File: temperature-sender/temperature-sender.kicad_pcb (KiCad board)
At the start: 2 copper layers, 50 x 25 mm, 43 parts, among them IC1 ATTINY2313A-S, K1 SERVO, P1 CONN_01X02, P2 CONN_01X02, P3 CONN_01X02, P6 ISP, P7 CONN_01X03, P8 CONN_01X03, SW1 SW_PUSH, SW2 SW_PUSH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

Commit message: Some more changes, slowly getting there
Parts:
- removed P6: ISP, Socket_Strips:Socket_Strip_Straight_2x03
- removed P7, P8: CONN_01X03, kicad-footprints:Pin_Header_Angled_SMD_1x03
- removed TP_PB0, TP_PB4, TP_PD4, TP_PD5, TP_PD6: TEST_POINT, kicad-footprints:TP_1mm
- removed U4: HT7550-1, Housings_SOT-89:SOT89-3_Housing_Handsoldering
- added C10: 0.1uF, Capacitors_SMD:C_0603_HandSoldering, B.Cu at (143.0, 148.5)
- added C8: 10uF, Capacitors_SMD:C_0603_HandSoldering, F.Cu at (139.5, 138.5)
- added C9: 10uF, Capacitors_SMD:C_0603_HandSoldering, F.Cu at (133.7, 144.8)
- added P4: CONN_01X04, kicad-footprints:Pin_Header_Angled_SMD_1x04, F.Cu at (109.3, 141.5)
- added P5: CONN_01X03, kicad-footprints:Pin_Header_Angled_SMD_1x03, F.Cu at (144.4, 134.6)
- added R1: 47k, Resistors_SMD:R_0603_HandSoldering, B.Cu at (136.3, 109.6)
- added R10: 5k, Resistors_SMD:R_0603_HandSoldering, F.Cu at (117.2, 145.5)
- added TP_PB2: TEST_POINT, kicad-footprints:TP_1mm, B.Cu at (123.7, 139.9)
- added TP_PB3: TEST_POINT, kicad-footprints:TP_1mm, B.Cu at (127.5, 144.7)
- added TP_PD1: TEST_POINT, kicad-footprints:TP_1mm, B.Cu at (123.8, 135.4)
- added TP_PD2: TEST_POINT, kicad-footprints:TP_1mm, B.Cu at (122.3, 135.4)
- C1: value 10uF -> 1uF
- C2, C4: value 1uF -> 10uF
- C3: value C -> 0.1uF; moved to B.Cu
- C5, C7: value 0.1uF -> 10uF
- P1: value CONN_01X02 -> ISP; footprint kicad-footprints:Pin_Header_Angled_SMD_1x02 -> Socket_Strips:Socket_Strip_Straight_2x03
- P3: value CONN_01X02 -> CONN_01X03; footprint kicad-footprints:Pin_Header_Angled_SMD_1x02 -> kicad-footprints:Pin_Header_Angled_SMD_1x03; moved to B.Cu
- R3: value 5k -> 240R
- R4: value 47R -> 1k5
- R5, R6: value 47k -> 47R
- R7: value 5k -> 47k; moved to B.Cu
- R9: value 47R -> 5k
- SW1, SW2: footprint Buttons_Switches_SMD:SW_SPST_PTS645 -> kicad-footprints:4x4x1.5mm_Tactile_Push_Button_SMD; moved to B.Cu
- U1: value MCP1700T-3302E/TT -> AMS1117; footprint Housings_SOT-23_SOT-143_TSOT-6:SOT-23_Handsoldering -> kicad-footprints:SOT-223
- U2: value TMP102 -> LM317L; footprint kicad-footprints:SOT563 -> Housings_TO-92:TO-92_Inline_Narrow_Oval
- U3: value 78L09 -> TMP102; footprint Housings_TO-92:TO-92_Inline_Narrow_Oval -> kicad-footprints:SOT563
- moved C5 101.0 mm to (106.3, 105.5), turned to 0 degrees
- moved C7 87.1 mm to (106.2, 103.6)
- moved R8 76.3 mm to (130.1, 146.7), turned to 180 degrees
- moved R4 59.8 mm to (104.9, 114.9)
- moved R5 58.8 mm to (139.1, 134.4), turned to 180 degrees
- moved R9 54.4 mm to (125.7, 148.4), turned to 270 degrees
- moved R7 52.4 mm to (140.9, 152.8)
- moved C3 41.6 mm to (136.1, 113.9)
- moved R3 40.9 mm to (104.9, 113.0), turned to 0 degrees
- moved U2 40.7 mm to (105.2, 110.5), turned to 90 degrees
- moved U3 34.3 mm to (120.7, 148.5)
- moved P2 31.9 mm to (94.7, 110.8)
- moved C6 28.2 mm to (106.2, 101.5), turned to 0 degrees
- moved C1 27.2 mm to (103.3, 104.5)
- moved P1 26.2 mm to (114.6, 139.6), turned to 90 degrees
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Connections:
- C1 pad 1: +5V -> /Vin_rec
- C3 pad 1: /SERVO_PWR -> GND
- C3 pad 2: GND -> /SW
- C4 pad 1: Net-(C4-Pad1) -> /9v
- C5 pad 1: /RESET -> /9v
- C6 pad 1: +9V -> /9v
- C7 pad 1: GND -> /9v
- C7 pad 2: Net-(C7-Pad2) -> GND
- D1 pad 1: Net-(C4-Pad1) -> /Vin_rec
- D1 pad 2: Net-(D1-Pad2) -> /Vin1
- D2 pad 1: Net-(D2-Pad1) -> /Vin_rec
- D2 pad 2: GND -> /Vin2
- D4 pad 1: Net-(D1-Pad2) -> /Vin2
- D5 pad 1: Net-(C4-Pad1) -> /Vin1
- D5 pad 2: Net-(D2-Pad1) -> GND
- IC1 pad 7: Net-(IC1-Pad7) -> /SW
- K1 pad 3: Net-(K1-Pad3) -> /SERVO_SIG
- P1 pad 1: Net-(D2-Pad1) -> /MISO
- P1 pad 2: Net-(D1-Pad2) -> +3V3
- P2 pad 1: /SDA/MOSI -> /Vin2
- P2 pad 2: /SCL -> /Vin1
- P3 pad 2: +3V3 -> /TX
- R3 pad 1: /ALERT -> /Vadj
- R3 pad 2: +3V3 -> /9v
- R4 pad 1: Net-(K1-Pad3) -> GND
- R4 pad 2: /SERVO1 -> /Vadj
- R5 pad 1: +3V3 -> /SERVO_SIG
- R5 pad 2: /RESET -> /SERVO1
- R6 pad 1: +3V3 -> /SERVO_PWR
- R6 pad 2: Net-(C7-Pad2) -> +3V3
- R7 pad 2: /SCL -> /RESET
- R9 pad 1: /SERVO_PWR -> +3V3
- R9 pad 2: +3V3 -> /SCL
- SW1 pad 1: GND -> /SW
- SW1 pad 2: /RESET -> GND
- SW2 pad 1: Net-(C7-Pad2) -> GND
- SW2 pad 2: GND -> /RESET
- TP_PB1 pad 1: Net-(IC1-Pad13) -> Net-(IC1-Pad12)
- TP_PD3 pad 1: Net-(IC1-Pad7) -> Net-(IC1-Pad11)
- TP_XTAL1 pad 1: Net-(IC1-Pad5) -> Net-(IC1-Pad4)
- TP_XTAL2 pad 1: Net-(IC1-Pad4) -> Net-(IC1-Pad5)
- U1 pad 3: +5V -> /9v
- U2 pad 1: /SCL -> /Vadj
- U2 pad 2: GND -> /9v
- U2 pad 3: /ALERT -> /Vin_rec
- U3 pad 1: +9V -> /SCL
- U3 pad 3: Net-(C4-Pad1) -> /ALERT

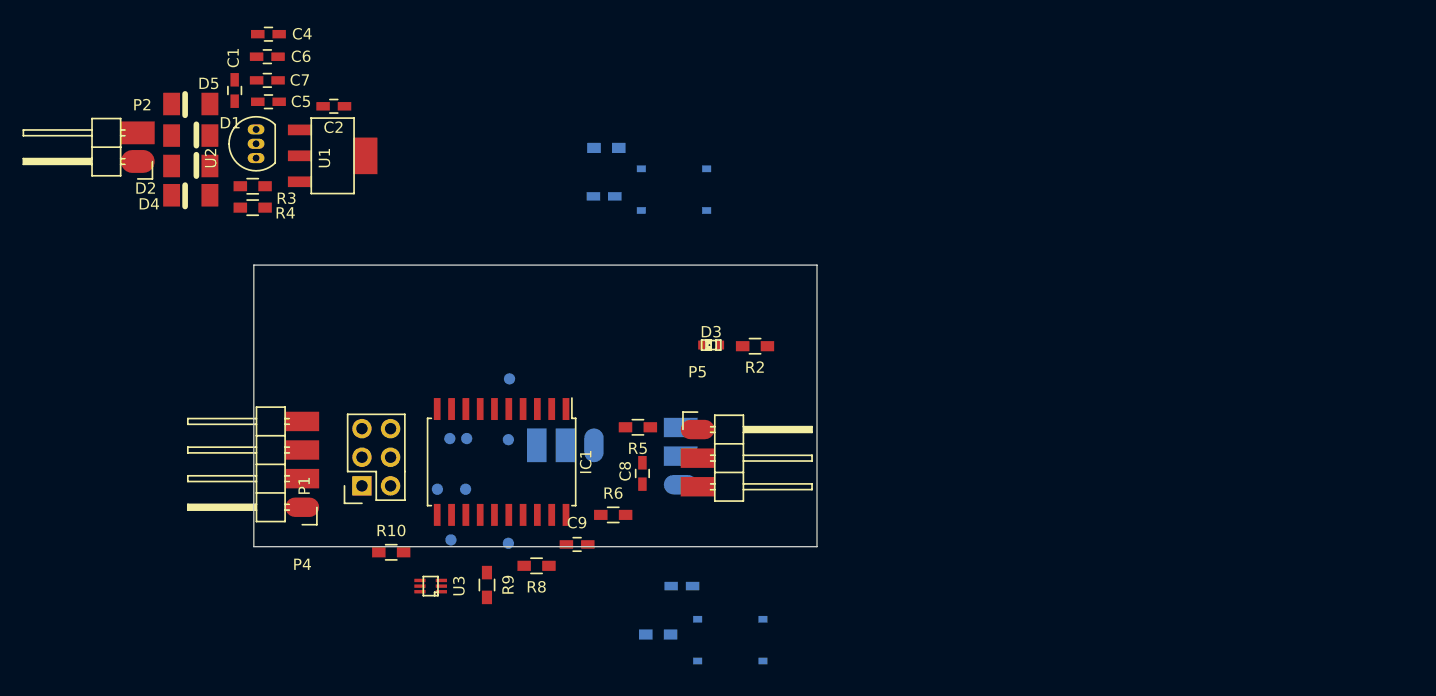
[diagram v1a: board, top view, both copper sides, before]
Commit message: Components placement mostly done
Problem with small temperature footprint. I like to have wider
power traces, but then it can't route this chip. Must figure out how
to solve it in KiCad.
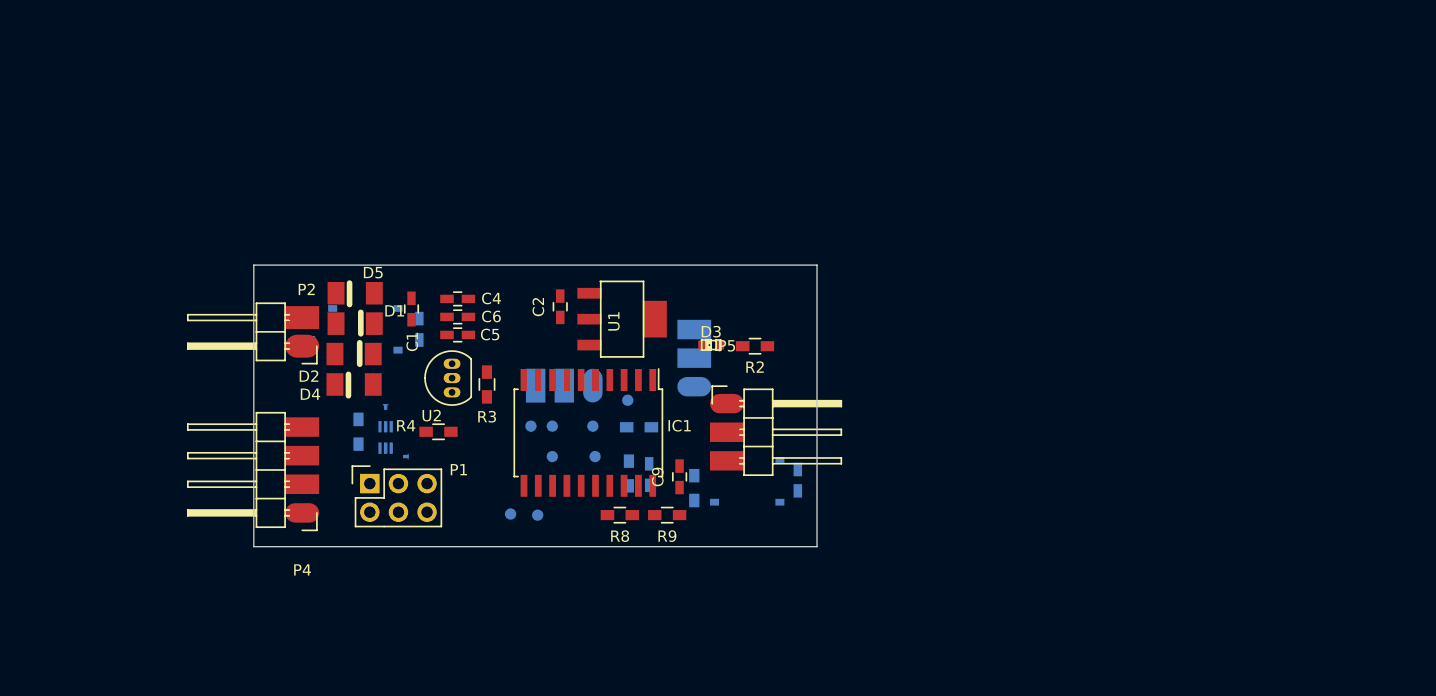
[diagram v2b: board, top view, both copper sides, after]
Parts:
- removed C7: 10uF, Capacitors_SMD:C_0603_HandSoldering
- added P6: 03mmTo05mm, kicad-footprints:03mmTo05mm, B.Cu at (116.7, 132.7)
- added P7: 03mmTo05mm, kicad-footprints:03mmTo05mm, B.Cu at (118.4, 137.0)
- C8, R10, R5, R6, U3: moved to B.Cu
- moved SW2 42.6 mm to (114.9, 125.7)
- moved R7 41.0 mm to (110.0, 125.8), turned to 90 degrees
- moved C10 32.6 mm to (119.7, 125.7), turned to 270 degrees
- moved R1 31.2 mm to (144.1, 139.8), turned to 270 degrees
- moved C3 30.5 mm to (153.3, 139.1), turned to 270 degrees
- moved U1 29.5 mm to (137.7, 124.8)
- moved C4 28.9 mm to (123.1, 123.0)
- moved C6 28.6 mm to (123.1, 124.6)
- moved R3 27.2 mm to (125.7, 130.6), turned to 90 degrees
- moved U2 27.1 mm to (122.6, 131.3)
- moved C2 26.8 mm to (132.2, 123.7), turned to 90 degrees
- moved SW1 26.7 mm to (148.8, 139.2)
- moved C5 26.7 mm to (123.1, 126.2)
- moved R4 25.9 mm to (121.4, 134.8), turned to 0 degrees
- moved C1 25.0 mm to (119.0, 123.9), turned to 90 degrees
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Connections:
- R10 pad 2: +3V3 -> /03mm3.3V
- U3 pad 2: GND -> Net-(P7-Pad1)
- U3 pad 4: +3V3 -> /03mm3.3V
- U3 pad 5: +3V3 -> /03mm3.3V
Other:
- net class 3V3 added: clearance 0.2, trace_width 0.25, via_dia 0.6, via_drill 0.4
- net class Default: clearance 0.2 -> 0.199
- net class GND added: clearance 0.2, trace_width 0.25, via_dia 0.6, via_drill 0.4
- net class POWER added: clearance 0.2, trace_width 0.5, via_dia 0.6, via_drill 0.4
- rule trace_clearance: 0.2 -> 0.199

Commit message: Temperature sender before import freerouting results
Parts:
- removed P6, P7: 03mmTo05mm, kicad-footprints:03mmTo05mm
- removed TP_PB2: TEST_POINT, kicad-footprints:TP_1mm
- removed U3: TMP102, kicad-footprints:SOT563
- added D6: Led_Small, LEDs:LED-0603, F.Cu at (126.9, 142.4)
- added GND1: TEST_POINT, Wire_Pads:SolderWirePad_single_1mmDrill, F.Cu at (151.0, 122.1)
- P4: value CONN_01X04 -> CONN_01X05; footprint kicad-footprints:Pin_Header_Angled_SMD_1x04 -> kicad-footprints:Pin_Header_Angled_SMD_1x05
- R10: value 5k -> 330R; moved to F.Cu
- moved R10 17.7 mm to (130.4, 142.2), turned to 180 degrees
- moved TP_XTAL2 5.78 mm to (140.3, 132.0)
- moved C1 1.10 mm to (120.1, 123.9)
- moved C5 1.00 mm to (124.1, 126.1)
- moved C4 1.00 mm to (124.1, 122.9)
- moved C6 1.00 mm to (124.1, 124.5)
- moved C8 0.91 mm to (141.0, 138.5)
- moved D2 0.70 mm to (114.6, 127.9)
- moved D4 0.70 mm to (114.6, 130.6)
- moved D1 0.54 mm to (114.5, 125.0)
- moved R4 0.51 mm to (121.3, 135.3)
- moved D5 0.51 mm to (114.5, 122.4)
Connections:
- R10 pad 1: /ALERT -> Net-(IC1-Pad13)
- R10 pad 2: /03mm3.3V -> Net-(D6-Pad2)
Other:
- net class 3V3: trace_width 0.25 -> 0.5
- net class GND: trace_width 0.25 -> 0.5

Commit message: Unknown changes, probably what I ordered
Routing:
- net GND: track 0.00 -> 184.1 mm, vias 0 -> 1
- net +3V3: track 0.00 -> 109.8 mm, vias 0 -> 1
- net /SW: track 0.00 -> 55.1 mm, vias 0 -> 1
- net /RESET: track 0.00 -> 53.1 mm, vias 0 -> 1
- net /SCL: track 0.00 -> 39.4 mm
- net /SDA/MOSI: track 0.00 -> 36.9 mm
- net /ALERT: track 0.00 -> 29.7 mm
- net /MISO: track 0.00 -> 25.7 mm, vias 0 -> 1
- net /9v: track 0.00 -> 20.9 mm
- net /RF_DATA: track 0.00 -> 20.7 mm
- net /SERVO_PWR: track 0.00 -> 13.8 mm
- net /RX: track 0.00 -> 13.1 mm, vias 0 -> 1
- net /Vin_rec: track 0.00 -> 12.0 mm
- net /SERVO_SIG: track 0.00 -> 11.3 mm
- net /TX: track 0.00 -> 8.09 mm, vias 0 -> 1
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- added copper zone on F.Cu, net +3V3
- added copper zone on B.Cu, net GND
